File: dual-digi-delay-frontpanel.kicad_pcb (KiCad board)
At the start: 2 copper layers, 50.5 x 175 mm, 1 part

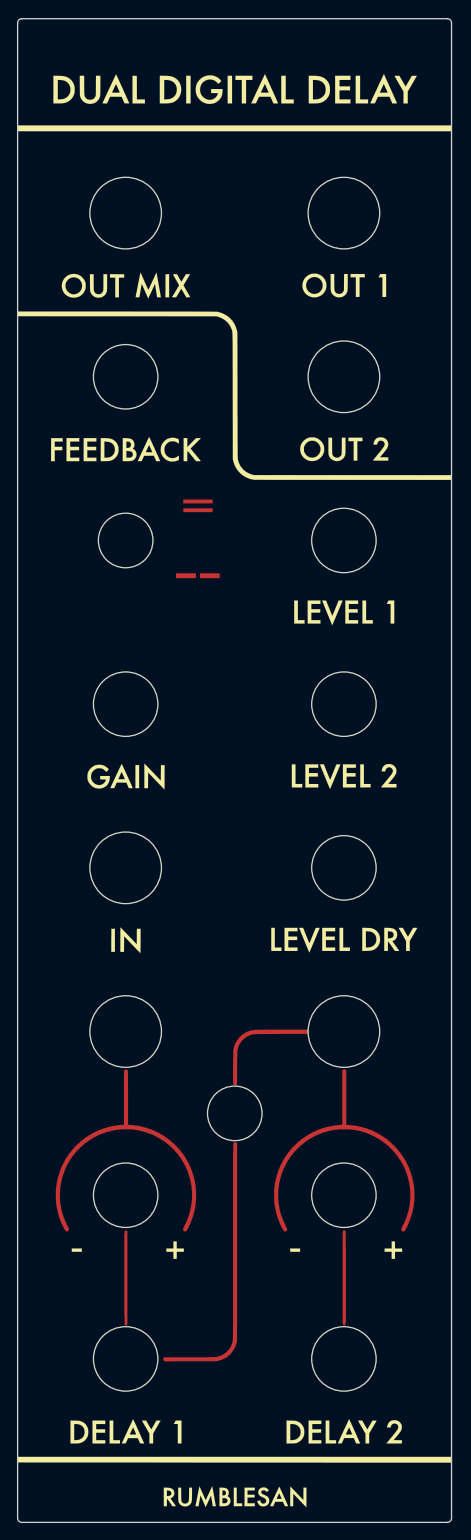
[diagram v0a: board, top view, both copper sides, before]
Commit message: Adding panel graphics files and kicad library
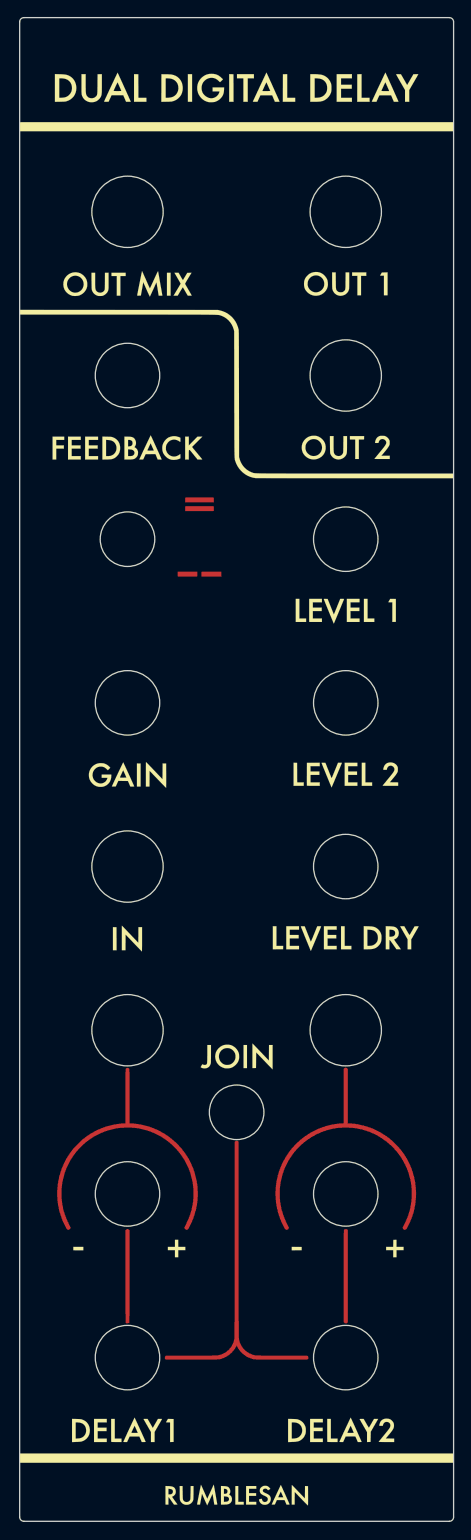
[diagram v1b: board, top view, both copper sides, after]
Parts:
- removed the Ref** at (102.2, 103.2)
- added Ref**: Val**, dual-pt2399-delay-panel:dual-pt2399-delay-4u-panel, F.Cu at (102.5, 103.1)
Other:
- net class Default removed
- net class Power removed
- net class Signal removed
